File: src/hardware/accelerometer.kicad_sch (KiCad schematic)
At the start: 16 parts

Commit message: Replaced schematics, 3d models and footprints. Added vibration motor.
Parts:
- removed U? (x4): LIS2DUX12TR, LGA-12_2.0X2.0X0.74_LIS2DUX12_STM, symbol LIS2DUX12TR:LIS2DUX12TR
- added U? (x4): LIS2DUX12TR, LGA-12_2.0X2.0X0.74_LIS2DUX12_STM, symbol LIS2DUX12TR:LIS2DUX12TR
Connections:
- net +1V8: now also U?.9 (VDD), U?.9 (VDD), U?.9 (VDD), U?.9 (VDD)
- net +3V3: now also U?.10 (VDD_IO), U?.10 (VDD_IO), U?.10 (VDD_IO), U?.10 (VDD_IO), U?.2 (CS), U?.2 (CS), U?.2 (CS), U?.2 (CS), U?.3 (SDO/SA0), U?.3 (SDO/SA0)
- net ACC1INT1: now also U?.12 (INT1)
- net ACC1INT2: now also U?.11 (INT2)
- net ACC2INT1: now also U?.12 (INT1)
- net ACC2INT2: now also U?.11 (INT2)
- net ACC3INT1: now also U?.12 (INT1)
- net ACC3INT2: now also U?.11 (INT2)
- net ACC4INT1: now also U?.12 (INT1)
- net ACC4INT2: now also U?.11 (INT2)
- net ACCCLK: now also U?.7 (RES), U?.7 (RES), U?.7 (RES), U?.7 (RES)
- net GND: now also U?.3 (SDO/SA0), U?.3 (SDO/SA0), U?.5 (NC), U?.5 (NC), U?.5 (NC), U?.5 (NC), U?.6 (GND), U?.6 (GND), U?.6 (GND), U?.6 (GND), U?.8 (GND), U?.8 (GND), U?.8 (GND), U?.8 (GND)
- net SCL: now also U?.1 (SCL/SPC), U?.1 (SCL/SPC)
- net SCL2: now also U?.1 (SCL/SPC), U?.1 (SCL/SPC)
- net SDA: now also U?.4 (SDA/SDI/SDO), U?.4 (SDA/SDI/SDO)
- net SDA2: now also U?.4 (SDA/SDI/SDO), U?.4 (SDA/SDI/SDO)

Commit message: Selected GPIO
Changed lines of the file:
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@@
 		)
 		(property "Value" "+3V3"
-			(at 88.9 54.6099 90)
-			(effects
-				(font
-					(size 1.27 1.27)
-				)
-				(justify left)
+			(at 91.44 52.07 90)
+			(effects
+				(font
+					(size 1.27 1.27)
+				)
 			)
 		)
@@
 		)
 		(property "Value" "GND"
-			(at 186.69 124.4599 90)
-			(effects
-				(font
-					(size 1.27 1.27)
-				)
-				(justify right)
+			(at 189.23 120.65 90)
+			(effects
+				(font
+					(size 1.27 1.27)
+				)
 			)
 		)
@@
 		)
 		(property "Value" "+3V3"
-			(at 88.9 114.2999 90)
-			(effects
-				(font
-					(size 1.27 1.27)
-				)
-				(justify left)
+			(at 91.44 111.76 90)
+			(effects
+				(font
+					(size 1.27 1.27)
+				)
 			)
 		)
@@
 		)
 		(property "Value" "+3V3"
-			(at 186.69 54.6099 90)
-			(effects
-				(font
-					(size 1.27 1.27)
-				)
-				(justify left)
+			(at 189.23 52.07 90)
+			(effects
+				(font
+					(size 1.27 1.27)
+				)
 			)
 		)
@@
 		)
 		(property "Value" "+3V3"
-			(at 186.69 114.2999 90)
-			(effects
-				(font
-					(size 1.27 1.27)
-				)
-				(justify left)
+			(at 189.23 111.76 90)
+			(effects
+				(font
+					(size 1.27 1.27)
+				)
 			)
 		)
@@
 		)
 		(property "Value" "+3V3"
-			(at 88.9 124.4599 90)
-			(effects
-				(font
-					(size 1.27 1.27)
-				)
-				(justify left)
+			(at 91.44 121.92 90)
+			(effects
+				(font
+					(size 1.27 1.27)
+				)
 			)
 		)
@@
 		)
 		(property "Value" "GND"
-			(at 186.69 64.7699 90)
-			(effects
-				(font
-					(size 1.27 1.27)
-				)
-				(justify right)
+			(at 189.23 60.96 90)
+			(effects
+				(font
+					(size 1.27 1.27)
+				)
 			)
 		)
@@
 		)
 		(property "Value" "+3V3"
-			(at 88.9 64.7699 90)
-			(effects
-				(font
-					(size 1.27 1.27)
-				)
-				(justify left)
-			)
-		)
+			(at 91.44 62.23 90)
+			(effects
+				(font
+					(size 1.27 1.27)
+				)
+			)
+		)

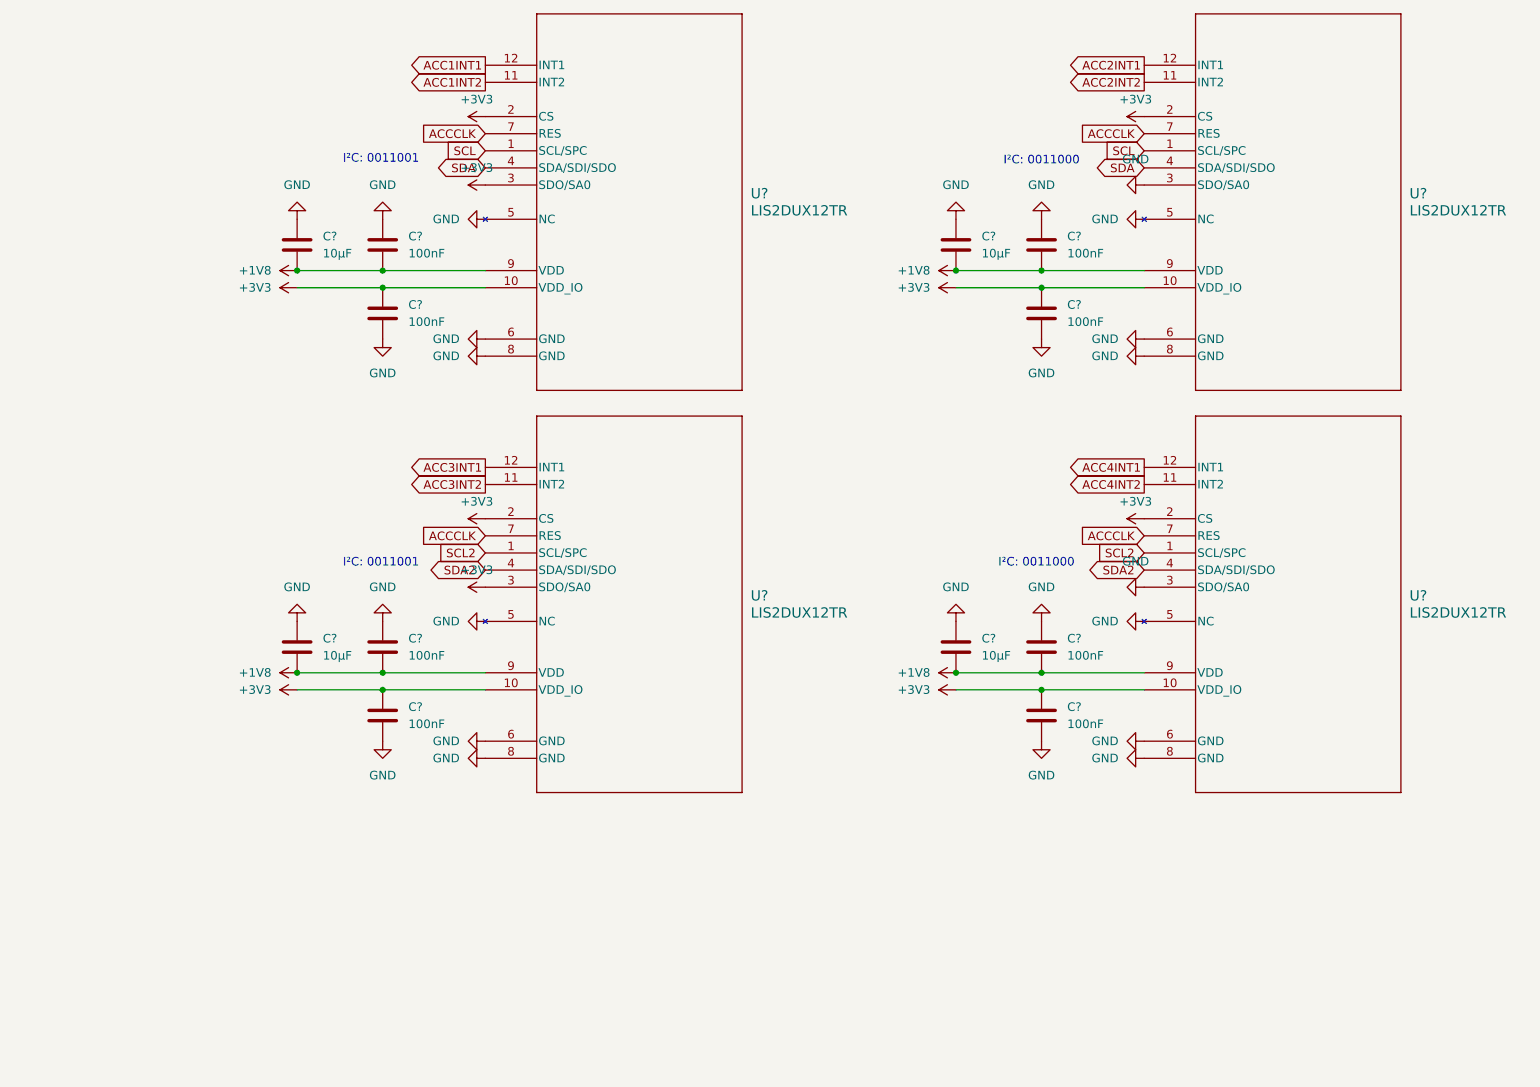
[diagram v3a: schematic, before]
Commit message: Added Accelerometer Clock; Cleanup & Fixes
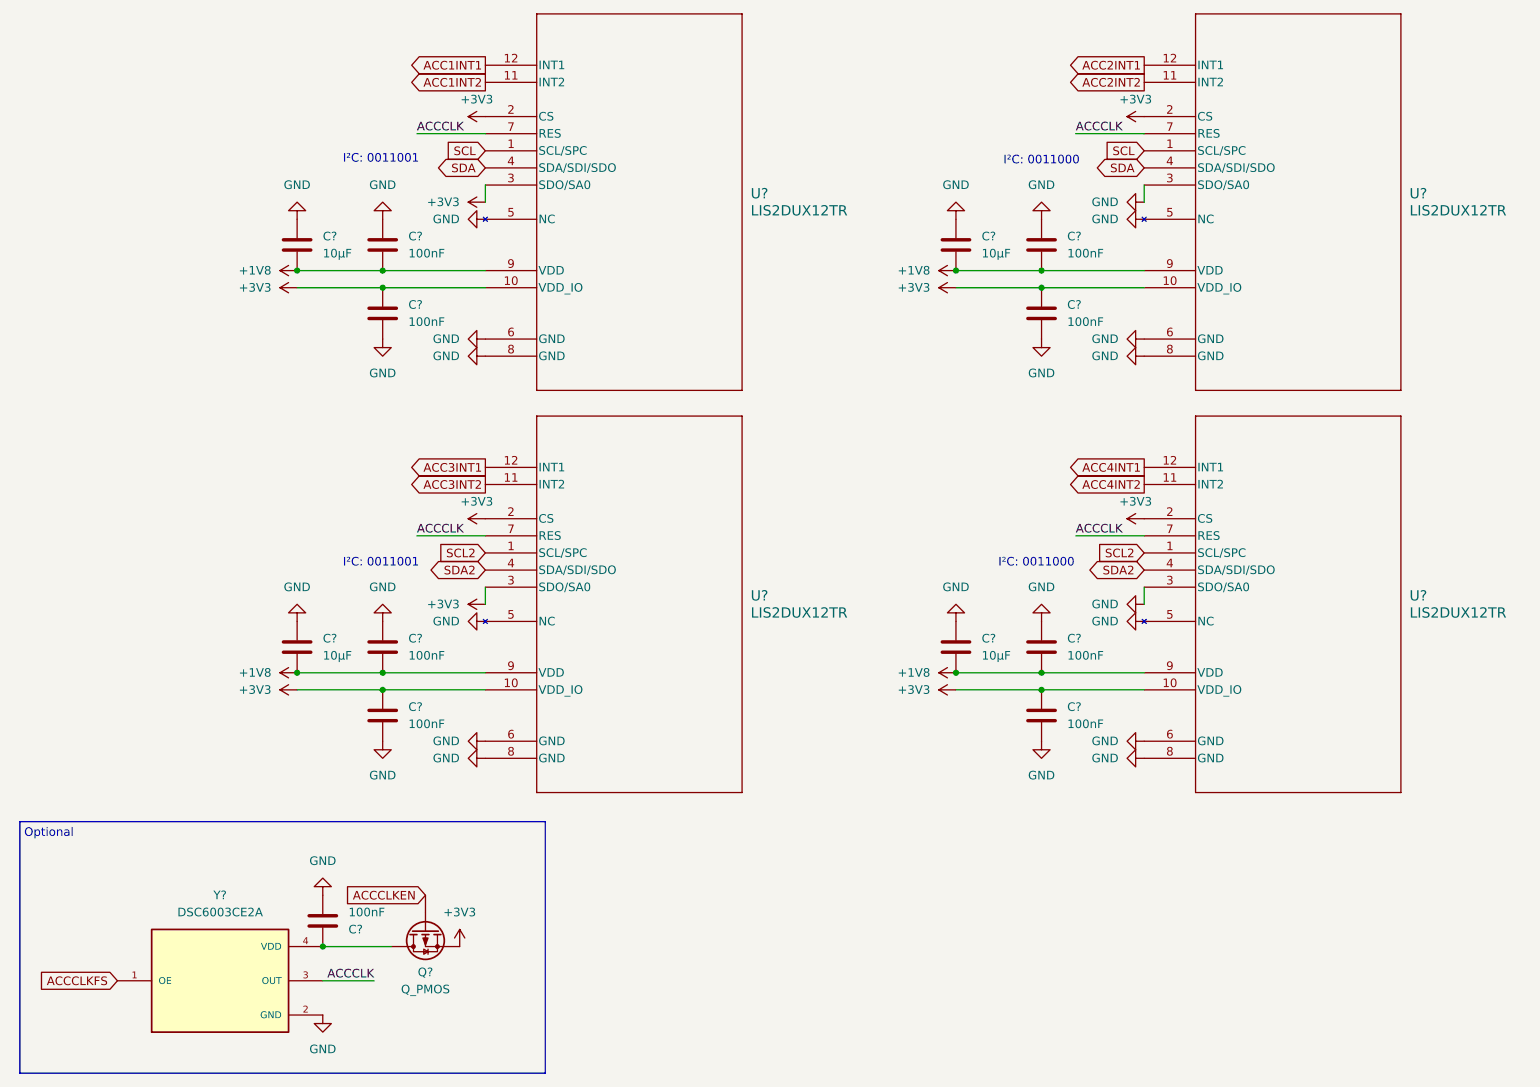
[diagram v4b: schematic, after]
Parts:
- added C?: 100nF, symbol Device:C
- added Q?: Q_PMOS, symbol Device:Q_PMOS
- added Y?: DSC6003CE2A, DSC6003CE2A-000.0000:OSC_DSC6003CE2A-000.0000, symbol DSC6003CE2A-000.0000:DSC6003CE2A-000.0000
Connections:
- net +3V3: now also Q?.S
- net ACCCLK: now also Y?.3 (OUT)
- net GND: now also C?.2, Y?.2 (GND)
- new net: C?.1, Q?.D, Y?.4 (VDD)
- new net ACCCLKEN: Q?.G
- new net ACCCLKFS: Y?.1 (OE)
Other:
- note added: "Optional"

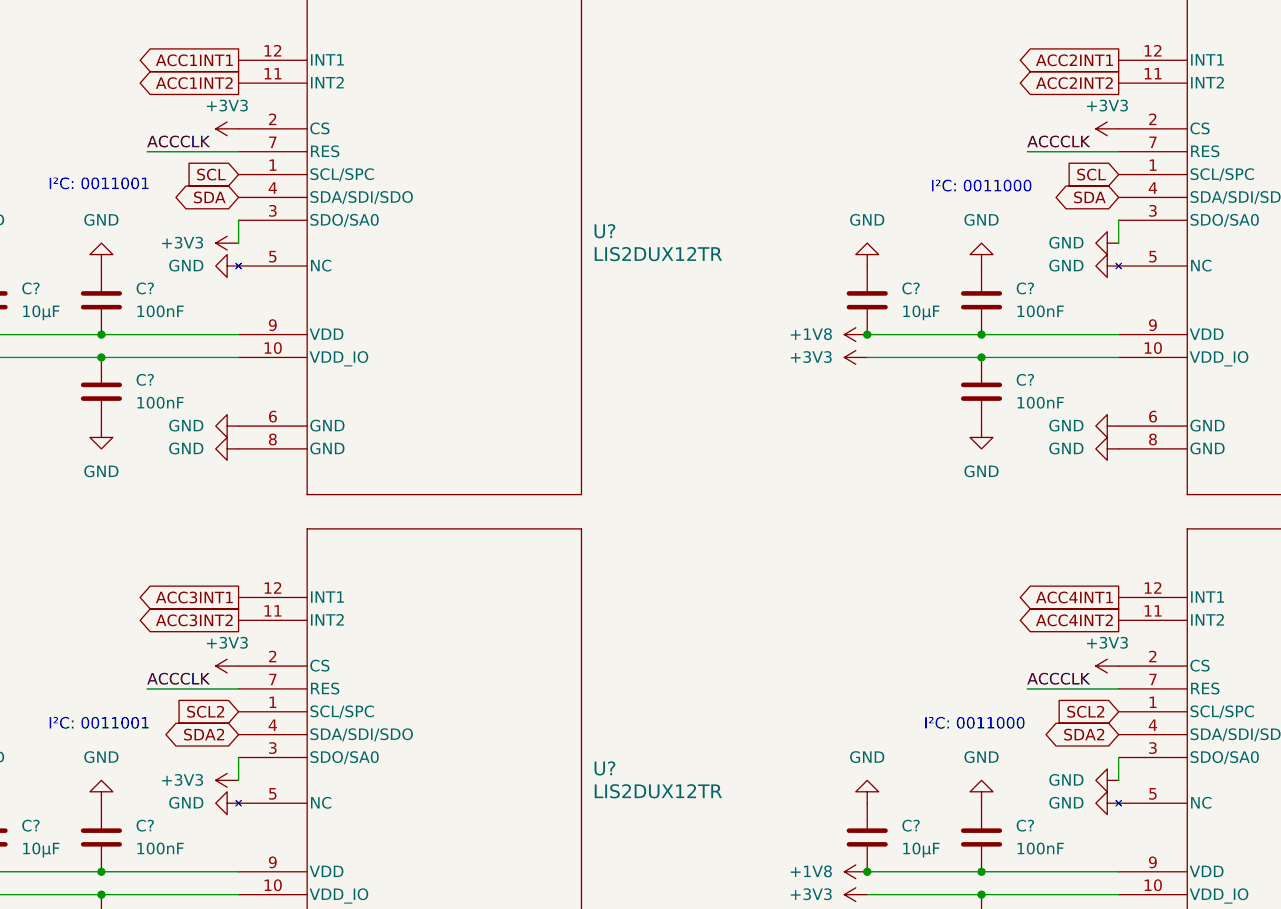
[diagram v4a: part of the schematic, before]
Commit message: Switched accelerometer I²C
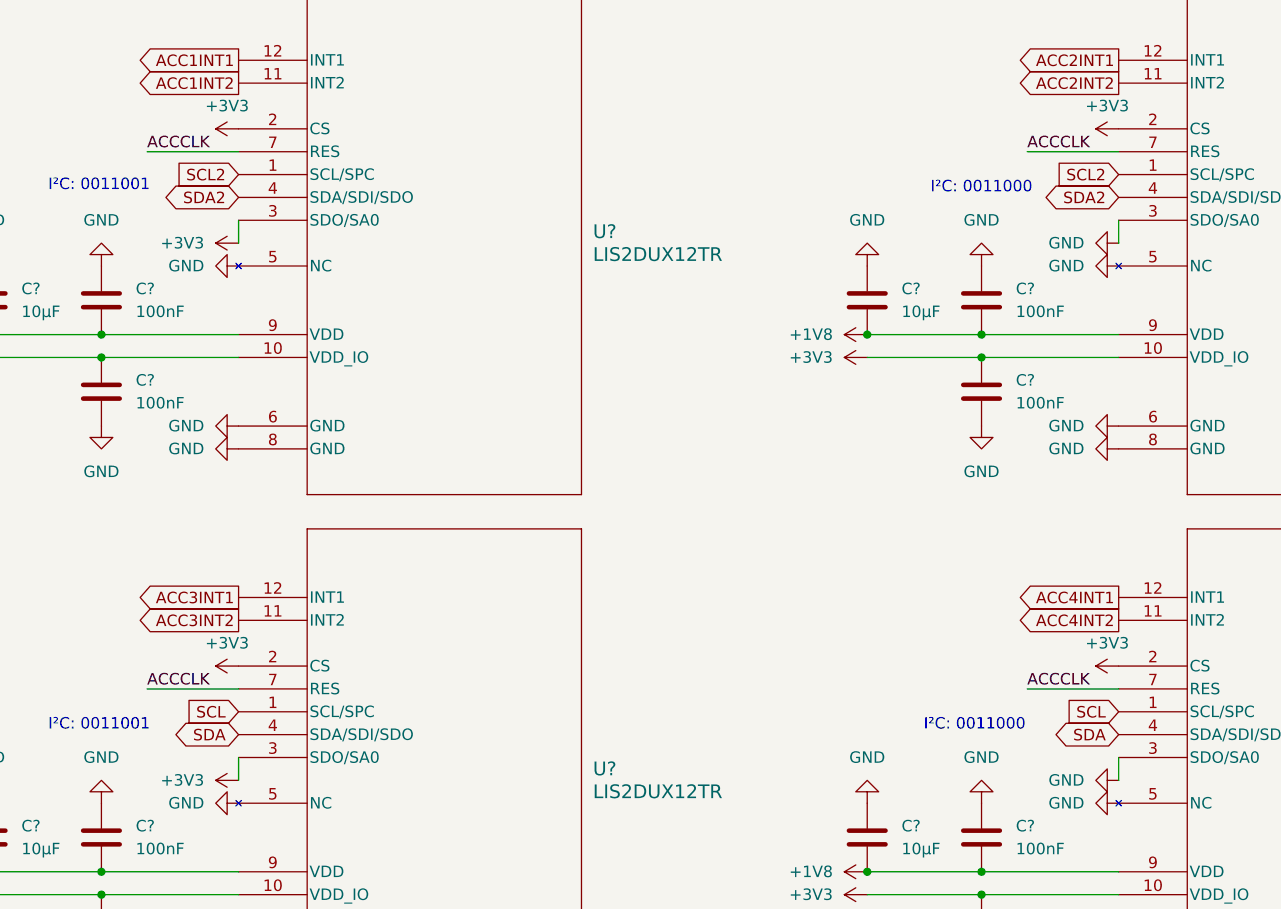
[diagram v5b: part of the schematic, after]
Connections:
- net SCL: now also U?.1 (SCL/SPC), U?.1 (SCL/SPC); no longer U?.1 (SCL/SPC), U?.1 (SCL/SPC)
- net SCL2: now also U?.1 (SCL/SPC), U?.1 (SCL/SPC); no longer U?.1 (SCL/SPC), U?.1 (SCL/SPC)
- net SDA: now also U?.4 (SDA/SDI/SDO), U?.4 (SDA/SDI/SDO); no longer U?.4 (SDA/SDI/SDO), U?.4 (SDA/SDI/SDO)
- net SDA2: now also U?.4 (SDA/SDI/SDO), U?.4 (SDA/SDI/SDO); no longer U?.4 (SDA/SDI/SDO), U?.4 (SDA/SDI/SDO)
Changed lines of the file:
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@@
 	(global_label "SCL"
 		(shape input)
-		(at 92.71 59.69 180)
-		(fields_autoplaced yes)
-		(effects
-			(font
-				(size 1.27 1.27)
-			)
-			(justify right)
-		)
-		(property "Intersheetrefs" "${INTERSHEET_REFS}"
-			(at 86.2172 59.69 0)
+		(at 92.71 119.38 180)
+		(fields_autoplaced yes)
+		(effects
+			(font
+				(size 1.27 1.27)
+			)
+			(justify right)
+		)
+		(property "Intersheetrefs" "${INTERSHEET_REFS}"
+			(at 86.2172 119.38 0)
 			(effects
 				(font
@@
 	(global_label "SDA"
 		(shape bidirectional)
-		(at 92.71 62.23 180)
-		(fields_autoplaced yes)
-		(effects
-			(font
-				(size 1.27 1.27)
-			)
-			(justify right)
-		)
-		(property "Intersheetrefs" "${INTERSHEET_REFS}"
-			(at 85.0454 62.23 0)
+		(at 92.71 121.92 180)
+		(fields_autoplaced yes)
+		(effects
+			(font
+				(size 1.27 1.27)
+			)
+			(justify right)
+		)
+		(property "Intersheetrefs" "${INTERSHEET_REFS}"
+			(at 85.0454 121.92 0)
 			(effects
 				(font
@@
 	(global_label "SDA2"
 		(shape bidirectional)
-		(at 92.71 121.92 180)
-		(fields_autoplaced yes)
-		(effects
-			(font
-				(size 1.27 1.27)
-			)
-			(justify right)
-		)
-		(property "Intersheetrefs" "${INTERSHEET_REFS}"
-			(at 83.8359 121.92 0)
+		(at 92.71 62.23 180)
+		(fields_autoplaced yes)
+		(effects
+			(font
+				(size 1.27 1.27)
+			)
+			(justify right)
+		)
+		(property "Intersheetrefs" "${INTERSHEET_REFS}"
+			(at 83.8359 62.23 0)
 			(effects
 				(font
@@
 	(global_label "SCL2"
 		(shape input)
-		(at 92.71 119.38 180)
-		(fields_autoplaced yes)
-		(effects
-			(font
-				(size 1.27 1.27)
-			)
-			(justify right)
-		)
-		(property "Intersheetrefs" "${INTERSHEET_REFS}"
-			(at 85.0077 119.38 0)
+		(at 92.71 59.69 180)
+		(fields_autoplaced yes)
+		(effects
+			(font
+				(size 1.27 1.27)
+			)
+			(justify right)
+		)
+		(property "Intersheetrefs" "${INTERSHEET_REFS}"
+			(at 85.0077 59.69 0)
 			(effects
 				(font
@@
 	(global_label "SCL2"
 		(shape input)
-		(at 190.5 119.38 180)
-		(fields_autoplaced yes)
-		(effects
-			(font
-				(size 1.27 1.27)
-			)
-			(justify right)
-		)
-		(property "Intersheetrefs" "${INTERSHEET_REFS}"
-			(at 182.7977 119.38 0)
+		(at 190.5 59.69 180)
+		(fields_autoplaced yes)
+		(effects
+			(font
+				(size 1.27 1.27)
+			)
+			(justify right)
+		)
+		(property "Intersheetrefs" "${INTERSHEET_REFS}"
+			(at 182.7977 59.69 0)
 			(effects
 				(font
@@
 	(global_label "SDA"
 		(shape bidirectional)
-		(at 190.5 62.23 180)
-		(fields_autoplaced yes)
-		(effects
-			(font
-				(size 1.27 1.27)
-			)
-			(justify right)
-		)
-		(property "Intersheetrefs" "${INTERSHEET_REFS}"
-			(at 182.8354 62.23 0)
+		(at 190.5 121.92 180)
+		(fields_autoplaced yes)
+		(effects
+			(font
+				(size 1.27 1.27)
+			)
+			(justify right)
+		)
+		(property "Intersheetrefs" "${INTERSHEET_REFS}"
+			(at 182.8354 121.92 0)
 			(effects
 				(font
@@
 	(global_label "SCL"
 		(shape input)
-		(at 190.5 59.69 180)
-		(fields_autoplaced yes)
-		(effects
-			(font
-				(size 1.27 1.27)
-			)
-			(justify right)
-		)
-		(property "Intersheetrefs" "${INTERSHEET_REFS}"
-			(at 184.0072 59.69 0)
+		(at 190.5 119.38 180)
+		(fields_autoplaced yes)
+		(effects
+			(font
+				(size 1.27 1.27)
+			)
+			(justify right)
+		)
+		(property "Intersheetrefs" "${INTERSHEET_REFS}"
+			(at 184.0072 119.38 0)
 			(effects
 				(font
@@
 	(global_label "SDA2"
 		(shape bidirectional)
-		(at 190.5 121.92 180)
-		(fields_autoplaced yes)
-		(effects
-			(font
-				(size 1.27 1.27)
-			)
-			(justify right)
-		)
-		(property "Intersheetrefs" "${INTERSHEET_REFS}"
-			(at 181.6259 121.92 0)
-			(effects
-				(font
+		(at 190.5 62.23 180)
+		(fields_autoplaced yes)
+		(effects
+			(font
+				(size 1.27 1.27)
+			)
+			(justify right)
+		)
+		(property "Intersheetrefs" "${INTERSHEET_REFS}"
+			(at 181.6259 62.23 0)
+			(effects
+				(font

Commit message: Cleanup & Fixes; Added footprints; Removed Light sensors
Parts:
- removed Q?: Q_PMOS, symbol Device:Q_PMOS
- added U12: TPS22916BYFPR, Project:IC_TPS22916BYFPR, symbol TPS22916BYFPR:TPS22916BYFPR
- C34, C35, C36, C37, C38, C39, C40, C41, C42, C43, C44, C45, C46: renamed from C?; footprint (none) -> Capacitor_SMD:C_0603_1608Metric
- U10, U11, U13, U14: renamed from U?; footprint LGA-12_2.0X2.0X0.74_LIS2DUX12_STM -> Project:LGA-12_2.0X2.0X0.74_LIS2DUX12_STM
- Y3: renamed from Y?; footprint DSC6003CE2A-000.0000:OSC_DSC6003CE2A-000.0000 -> Project:OSC_DSC6003CE2A-000.0000
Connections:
- net +3V3: now also U12.A2 (VIN)
- net ACCCLKEN: now also U12.B2 (ON)
- net GND: now also U12.B1 (GND)
- net at C36.1, Y3.4 (VDD): now also U12.A1 (VOUT)
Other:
- moved on the sheet: C36

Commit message: Cleanup & Fixes; Changed GPIO; Added Camera; Added Microphone
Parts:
- renumbered C34 to C32, C35 to C33, C36 to C34, C37 to C35, C38 to C36, C39 to C37, C40 to C38, C41 to C39, C42 to C40, C43 to C41, C44 to C42, C45 to C43, C46 to C44

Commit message: Add Light Sensor and Proximity & Gesture Sensor; Changed GPIO
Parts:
- renumbered U10 to U11, U11 to U12, U12 to U13, U13 to U14, U14 to U15
